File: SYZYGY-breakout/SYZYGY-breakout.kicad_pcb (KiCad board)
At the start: 2 copper layers, 40.5 x 51.7 mm, 12 parts, among them J1 QSH-020-01-X-D-DP-A, J2 Conn_02x20_Odd_Even, J3 Conn_02x20_Odd_Even, J4 Conn_01x02

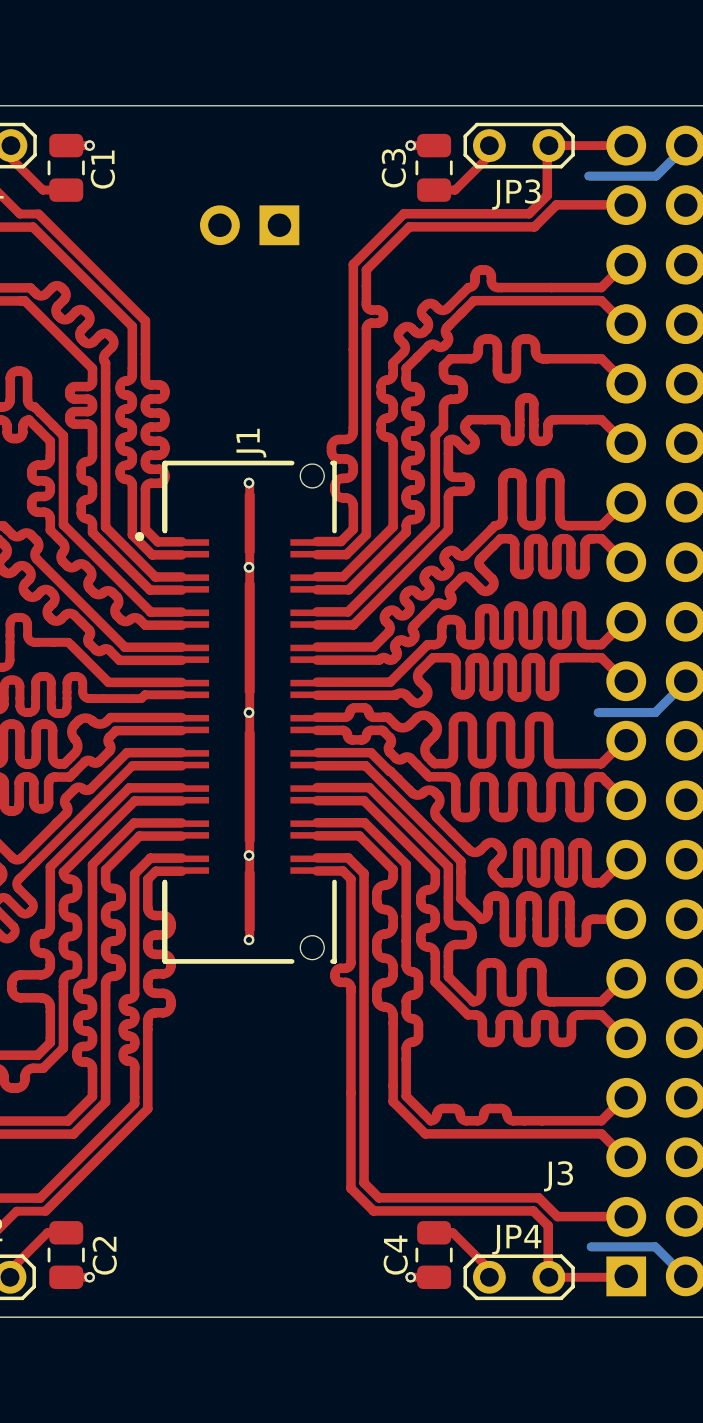
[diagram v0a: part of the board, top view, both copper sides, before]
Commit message: fixing length tuning
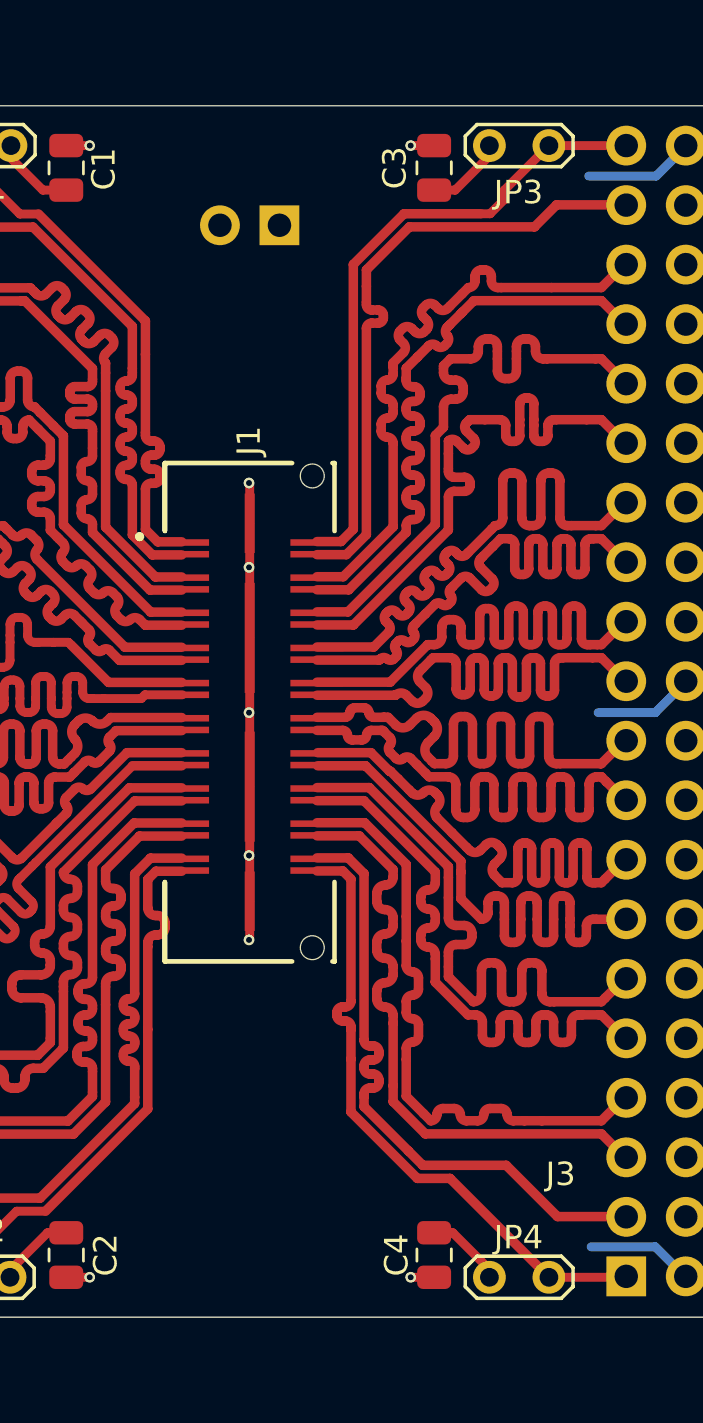
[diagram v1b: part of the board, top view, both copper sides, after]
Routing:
- net /D19-: track 30.3 -> 27.0 mm
- net /D0+: track 30.2 -> 26.9 mm
- net /D9-: track 30.1 -> 26.9 mm
- net /D10+: track 30.2 -> 27.1 mm
